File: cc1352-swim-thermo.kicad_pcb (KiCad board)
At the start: 4 copper layers, 49.4 x 41.9 mm, 73 parts, among them J1 LMT_70_1, J2 LMT_70_2, J3 SMA, J4 U.FL, J5 USB_B_Micro, J6 Conn_02x05_Odd_Even, Q1 2N7002, SW1 SW_Push, U1 0850BM14E0016T, U2 CC1352R1F3RGZR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

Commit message: PCB ready for manufacturing
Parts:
- removed TP1, TP10, TP11, TP12, TP13, TP14, TP15, TP16, TP17, TP18, TP19, TP2, TP3, TP4, TP5, TP6, TP7, TP8, TP9: TestPoint, TestPoint:TestPoint_Pad_D1.0mm
- added REF**: MountingHole_2.2mm_M2_DIN965_Pad, MountingHole:MountingHole_2.2mm_M2_DIN965_Pad, F.Cu at (124.9, 91.6)
- moved BT1 63.6 mm to (93.3, 124.7), turned to 0 degrees
- moved C10 53.5 mm to (104.5, 117.0), turned to 180 degrees
- moved C7 49.1 mm to (110.6, 121.3), turned to 270 degrees
- moved C8 47.6 mm to (104.5, 118.5), turned to 180 degrees
- moved L1 47.6 mm to (104.3, 115.3), turned to 180 degrees
- moved C4 45.0 mm to (108.9, 108.5), turned to 180 degrees
- moved R3 44.3 mm to (109.3, 95.5)
- moved J4 43.4 mm to (115.9, 125.5), turned to 270 degrees
- moved C34 41.8 mm to (117.5, 121.1), turned to 45 degrees
- moved J6 41.6 mm to (111.2, 99.5)
- moved C35 40.5 mm to (118.9, 121.8), turned to 135 degrees
- moved C5 36.9 mm to (108.9, 107.0), turned to 180 degrees
- moved C22 35.9 mm to (112.5, 95.5)
- moved C9 35.7 mm to (113.6, 121.3), turned to 270 degrees
- moved U1 34.3 mm to (116.7, 115.9)
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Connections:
- U2 pad 10: Net-(TP3-Pad1) -> (no net)
- U2 pad 11: Net-(TP4-Pad1) -> (no net)
- U2 pad 12: Net-(TP5-Pad1) -> (no net)
- U2 pad 14: /PSU_ENABLE -> /SWITCH
- U2 pad 15: /SWITCH -> /T_ON_1
- U2 pad 16: /LED_EASYSET -> /TAO_1
- U2 pad 17: /T_ON_1 -> /T_ON_2
- U2 pad 18: /TAO_1 -> /TAO_2
- U2 pad 19: /T_ON_2 -> /LED_EASYSET
- U2 pad 20: /TAO_2 -> /PSU_ENABLE
- U2 pad 21: Net-(TP10-Pad1) -> (no net)
- U2 pad 28: Net-(TP19-Pad1) -> (no net)
- U2 pad 29: Net-(TP16-Pad1) -> (no net)
- U2 pad 30: Net-(TP18-Pad1) -> (no net)
- U2 pad 31: Net-(TP17-Pad1) -> (no net)
- U2 pad 32: Net-(TP15-Pad1) -> (no net)
- U2 pad 36: Net-(TP14-Pad1) -> (no net)
- U2 pad 37: Net-(TP13-Pad1) -> (no net)
- U2 pad 38: Net-(TP12-Pad1) -> (no net)
- U2 pad 39: Net-(TP11-Pad1) -> (no net)
- U2 pad 40: Net-(TP9-Pad1) -> (no net)
- U2 pad 41: Net-(TP8-Pad1) -> (no net)
- U2 pad 42: Net-(TP7-Pad1) -> (no net)
- U2 pad 43: Net-(TP6-Pad1) -> (no net)
- U2 pad 8: Net-(TP1-Pad1) -> (no net)
- U2 pad 9: Net-(TP2-Pad1) -> (no net)
- U3 pad 2: GND -> (no net)
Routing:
- net GND: track 22.1 -> 55.5 mm, vias 124 -> 291
- net /RESET_N: track 0.00 -> 26.9 mm, vias 0 -> 2
- net /VDDR: track 0.00 -> 23.8 mm, vias 0 -> 2
- net /TAO_2: track 0.00 -> 23.2 mm
- net /T_ON_2: track 6.38 -> 28.9 mm, vias 0 -> 1
- net /TAO_1: track 0.00 -> 21.0 mm, vias 0 -> 1
- net /JTAG_TDI: track 0.00 -> 18.3 mm, vias 0 -> 2
- net /VDDS: track 4.30 -> 21.4 mm, vias 2 -> 8
- net /JTAG_TDO: track 0.00 -> 16.0 mm, vias 0 -> 2
- net /JTAG_TCKC: track 0.00 -> 13.5 mm, vias 0 -> 2
- net /SWITCH: track 35.2 -> 22.0 mm, vias 1 -> 2
- net /TAO: track 12.5 -> 0.00 mm
- net /LED_EASYSET: track 5.86 -> 18.0 mm
- net Net-(C33-Pad2): track 0.00 -> 11.3 mm
- net /JTAG_TMSC: track 0.00 -> 9.29 mm, vias 0 -> 2
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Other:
- board size 49.4 x 41.9 mm -> 49.8 x 41.8 mm
- board text added: "Sensor node/concentrator CC1352 sub-GHz and BLE @mik4el4ndersson v1.0"
- board text removed: "Sensor node/concentrator CC1350 sub-GHz and BLE @mik4el4ndersson v1.2"

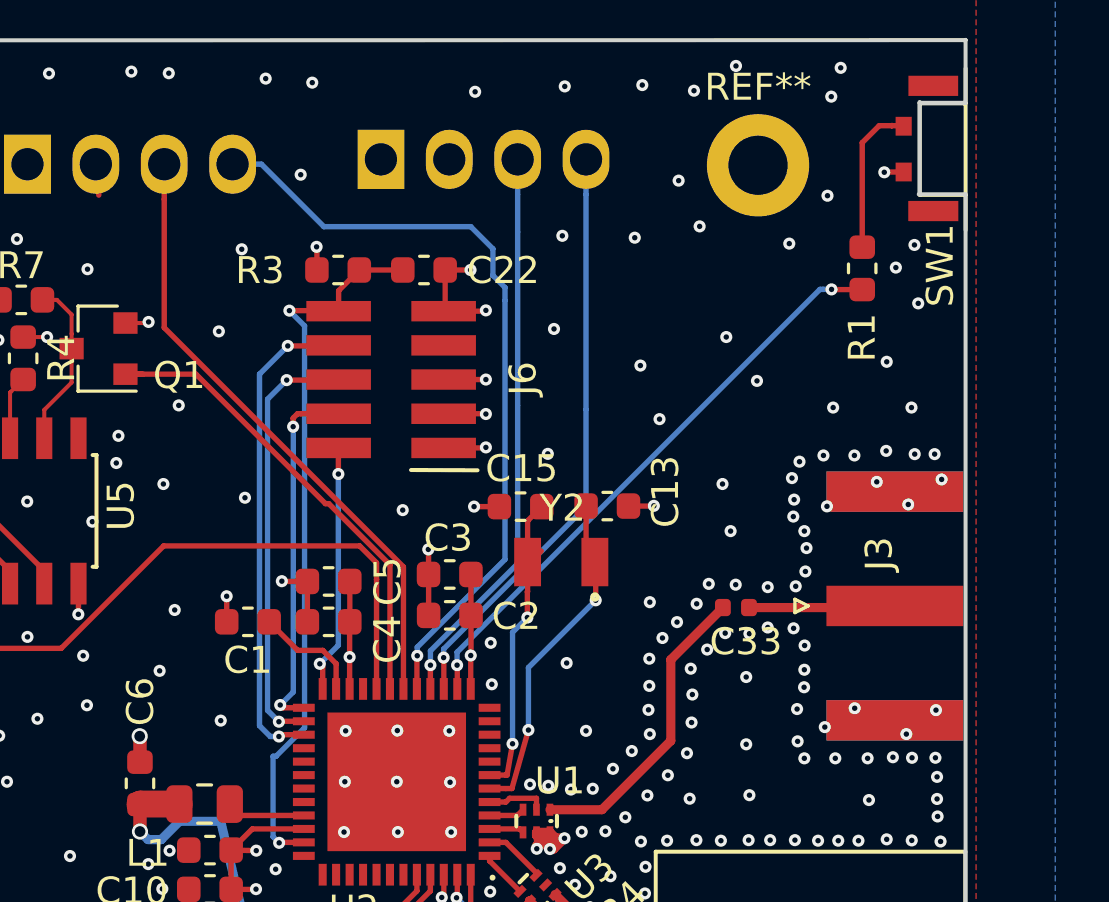
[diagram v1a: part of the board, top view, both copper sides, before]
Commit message: PCB sent to manufacturing
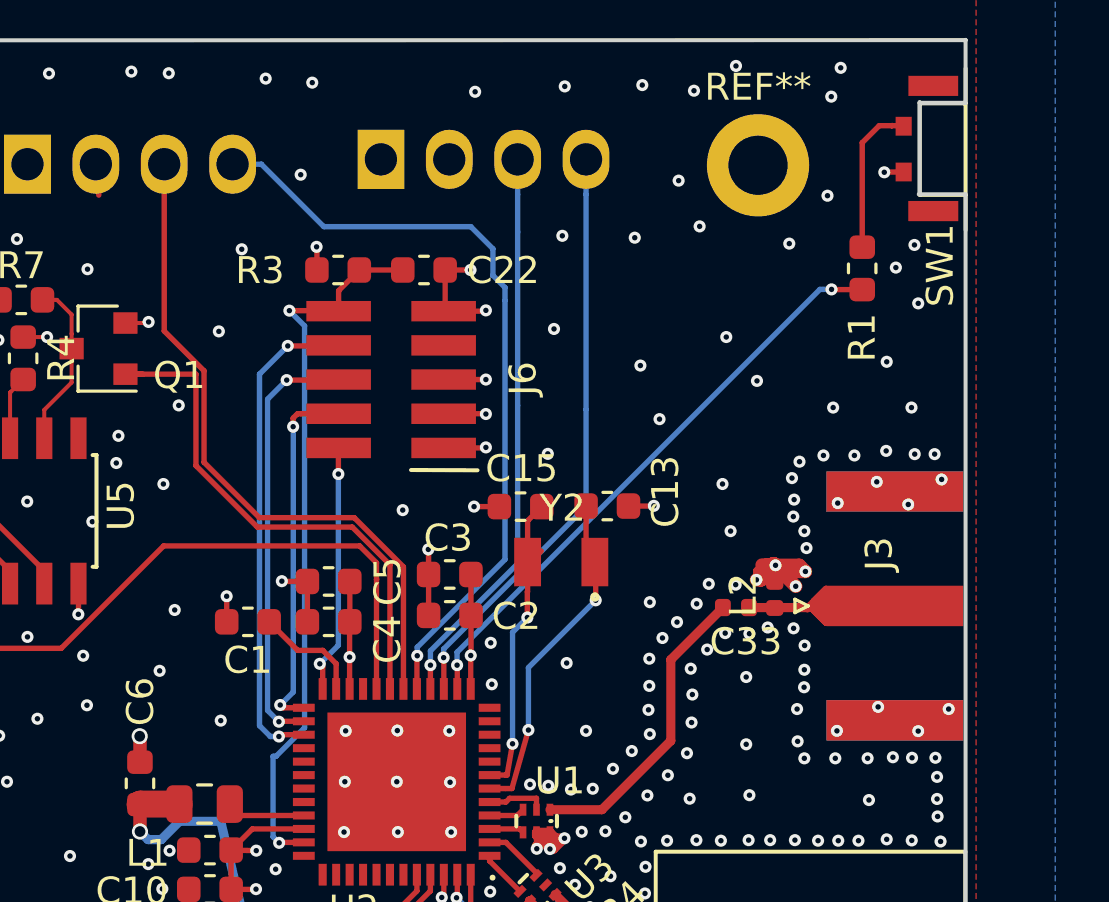
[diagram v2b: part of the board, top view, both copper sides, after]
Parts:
- added L2: DNM, Inductor_SMD:L_0402_1005Metric, F.Cu at (125.5, 107.5)
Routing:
- net GND: track 55.5 -> 63.8 mm
- net Net-(C33-Pad1): track 4.90 -> 10.5 mm
- net /TAO_2: track 23.2 -> 25.2 mm
- net /LED_EASYSET: track 18.0 -> 20.0 mm

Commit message: new rev of pcb
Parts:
- removed REF**: MountingHole_2.2mm_M2_DIN965_Pad, MountingHole:MountingHole_2.2mm_M2_DIN965_Pad
- C10, C11, C3, C5, C7, C9: value 0.1uF -> 100nF
- JP1: moved to B.Cu
- moved L6 17.0 mm to (106.2, 120.7), turned to 270 degrees
- moved Y1 5.75 mm to (112.0, 122.8), turned to 135 degrees
- moved C7 3.08 mm to (107.7, 120.1)
- moved C11 2.98 mm to (109.2, 120.5)
- moved C9 1.03 mm to (114.3, 120.6)
- turned JP1 to 270 degrees
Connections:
- J1 pad 1: /VDDS -> VCC
- J2 pad 1: /VDDS -> VCC
- J6 pad 1: /VDDS -> VCC
- R3 pad 1: /VDDS -> VCC
- U2 pad 10: (no net) -> /SWITCH
- U2 pad 11: (no net) -> /T_ON_1
- U2 pad 12: (no net) -> /T_ON_2
- U2 pad 14: /SWITCH -> (no net)
- U2 pad 15: /T_ON_1 -> (no net)
- U2 pad 16: /TAO_1 -> (no net)
- U2 pad 17: /T_ON_2 -> (no net)
- U2 pad 18: /TAO_2 -> (no net)
- U2 pad 36: (no net) -> /TAO_2
- U2 pad 37: (no net) -> /TAO_1
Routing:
- net VCC: track 50.5 -> 160.2 mm, vias 1 -> 4
- net /VDDS: track 21.4 -> 43.6 mm, vias 8 -> 3
- net /TAO_1: track 21.0 -> 31.0 mm
- net Net-(U2-Pad47): track 13.6 -> 5.30 mm, vias 2 -> 0
- net Net-(U2-Pad46): track 12.8 -> 5.78 mm, vias 2 -> 0
- net /VDDR: track 23.8 -> 27.8 mm, vias 2 -> 3
- net /TAO_2: track 25.2 -> 28.7 mm, vias 0 -> 1
- net /T_ON_2: track 28.9 -> 31.6 mm, vias 1 -> 2
- net /SWITCH: track 22.0 -> 23.9 mm
- net /T_ON_1: track 22.1 -> 23.3 mm
- net GND: track 63.8 -> 65.0 mm, vias 291 -> 288
- net Net-(C13-Pad1): track 13.2 -> 13.5 mm, vias 2 -> 0
- net Net-(C15-Pad1): vias 2 -> 0
- removed copper zone on In2.Cu, net /VDDS
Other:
- board text added: "Sensor node/concentrator CC1352 sub-GHz and BLE @mik4el4ndersson v1.1"
- board text removed: "Sensor node/concentrator CC1352 sub-GHz and BLE @mik4el4ndersson v1.0"
